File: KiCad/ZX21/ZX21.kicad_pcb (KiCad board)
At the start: 2 copper layers, 142 x 100 mm, 104 parts, among them IC1 ULA 2C210E, IC101 555, IC2 AT28C256, IC3 Z80A, IC301 3V3 PSU, IC303 AZ1117-3.3, IC4 62256, IC501 YM2149, IC502 GAL16V8, J1 Jack-DC, J203 Conn_01x03, J204 Conn_01x03, J301 Conn_01x04, J401 DB9_Male, J501 Conn_01x05, J502 Conn_01x08, J503 Conn_01x08, J504 Conn_01x07, J601 Conn_02x08_Odd_Even, J701 Conn_02x23_Row_Letter_First, J702 Conn_01x09, J703 Conn_01x09, X1 3.5MHz

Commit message: Diodes fixed
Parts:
- added D1: 1N4148, Diodes_THT:D_DO-35_SOD27_P7.62mm_Horizontal, F.Cu at (149.2, 118.1)
- added D101: 1N4148, Diodes_THT:D_DO-35_SOD27_P7.62mm_Horizontal, F.Cu at (43.2, 83.2)
- added D102: 1N4148, Diodes_THT:D_DO-35_SOD27_P7.62mm_Horizontal, F.Cu at (33.0, 83.2)
- added D2: 1N4148, Diodes_THT:D_DO-35_SOD27_P7.62mm_Horizontal, F.Cu at (151.8, 118.1)
- added D3: 1N4148, Diodes_THT:D_DO-35_SOD27_P7.62mm_Horizontal, F.Cu at (154.3, 118.1)
- added D4: 1N4148, Diodes_THT:D_DO-35_SOD27_P7.62mm_Horizontal, F.Cu at (156.8, 118.1)
- added D5: 1N4148, Diodes_THT:D_DO-35_SOD27_P7.62mm_Horizontal, F.Cu at (159.4, 118.1)
- added D6: 1N4148, Diodes_THT:D_DO-35_SOD27_P7.62mm_Horizontal, F.Cu at (161.9, 118.1)
- added D7: 1N4148, Diodes_THT:D_DO-35_SOD27_P7.62mm_Horizontal, F.Cu at (157.5, 118.7)
- added D8: 1N4148, Diodes_THT:D_DO-35_SOD27_P7.62mm_Horizontal, F.Cu at (167.0, 118.7)
- moved R28 245.5 mm to (161.9, 54.0)
- moved R33 165.0 mm to (73.0, 32.4)
- moved C7 164.3 mm to (83.2, 0.00)
- moved R4 147.0 mm to (97.2, 29.8)
- moved C10 142.1 mm to (103.6, 34.3)
- moved C6 136.9 mm to (78.1, 20.3)
- moved R101 130.7 mm to (62.2, 76.8), turned to 180 degrees
- moved R5 127.2 mm to (92.7, 19.1)
- moved C1 126.5 mm to (92.7, 95.2)
- moved C5 124.6 mm to (108.0, 90.8), turned to 270 degrees
- moved C2 105.2 mm to (9.53, 36.2)
- moved R103 89.7 mm to (56.5, 70.5)
- moved C103 73.6 mm to (47.6, 80.0)
- moved C12 70.3 mm to (53.3, 106.7), turned to 180 degrees
- moved C104 68.5 mm to (41.9, 78.7)
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
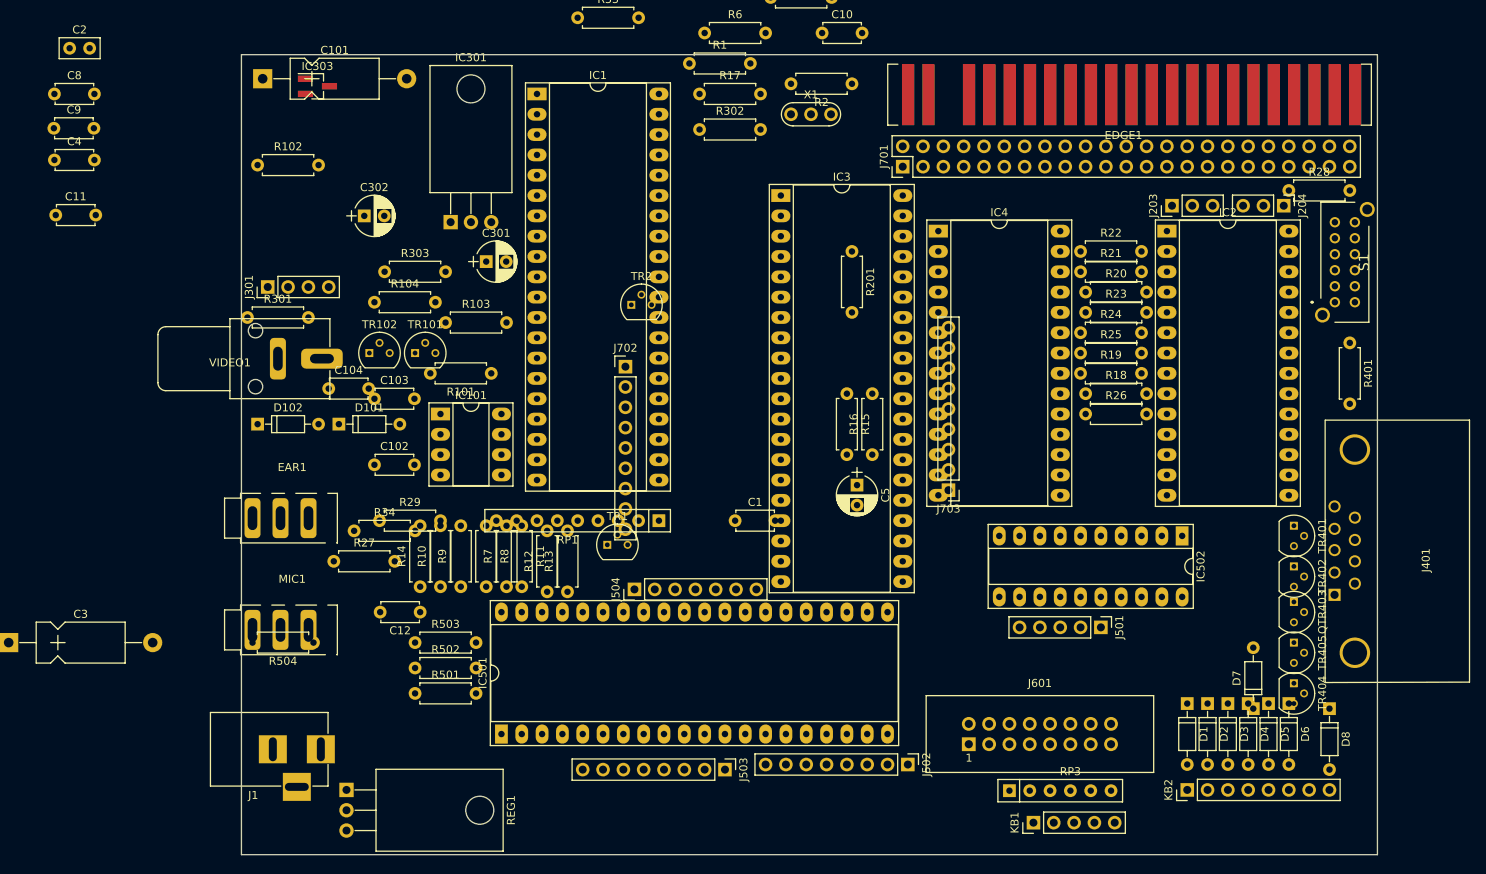
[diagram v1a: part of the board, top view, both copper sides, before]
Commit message: Added mounring holes
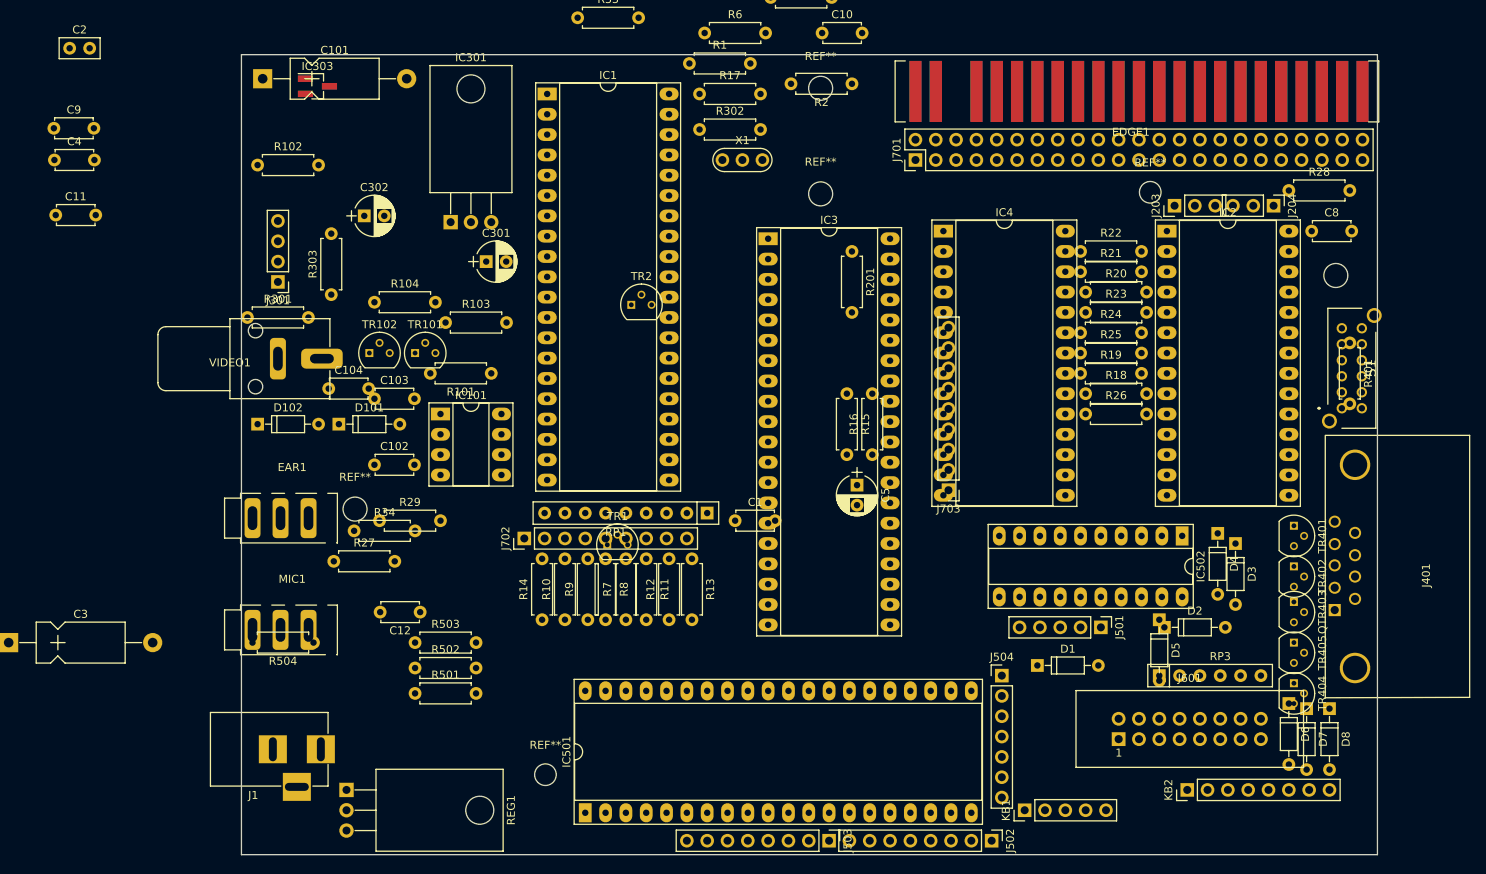
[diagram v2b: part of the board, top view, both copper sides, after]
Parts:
- added REF**: MountingHole_3mm, Mounting_Holes:MountingHole_3mm, F.Cu at (45.2, 93.8)
- added REF**: MountingHole_2.7mm, Mounting_Holes:MountingHole_2.7mm, F.Cu at (69.0, 127.0)
- added REF**: MountingHole_3mm, Mounting_Holes:MountingHole_3mm, F.Cu at (103.4, 54.4)
- added REF**: MountingHole_3mm, Mounting_Holes:MountingHole_3mm, F.Cu at (103.4, 41.2)
- added REF**: MountingHole_2.7mm, Mounting_Holes:MountingHole_2.7mm, F.Cu at (144.6, 54.2)
- added REF**: MountingHole_3mm, Mounting_Holes:MountingHole_3mm, F.Cu at (167.8, 64.6)
- moved C8 158.1 mm to (164.8, 59.1)
- moved J504 47.2 mm to (126.0, 114.6), turned to 0 degrees
- moved J702 24.9 mm to (66.4, 97.5), turned to 90 degrees
- moved RP3 23.6 mm to (145.7, 114.6)
- moved D4 21.6 mm to (153.0, 96.8)
- moved D3 20.0 mm to (155.3, 98.1)
- moved D1 19.3 mm to (130.5, 113.3), turned to 0 degrees
- moved J601 18.7 mm to (140.7, 122.6)
- moved D5 17.2 mm to (145.7, 107.6)
- moved R9 16.4 mm to (74.3, 107.6)
- moved R13 16.1 mm to (87.3, 100.0), turned to 270 degrees
- moved R10 16.1 mm to (71.4, 107.6)
- moved R11 16.1 mm to (81.6, 100.0)
- moved R14 15.8 mm to (68.6, 107.6)
- moved J503 15.8 mm to (104.5, 135.3)
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
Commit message: Placement getting there
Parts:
- removed REF** (x4): MountingHole_3mm, Mounting_Holes:MountingHole_3mm
- removed REF** (x2): MountingHole_2.7mm, Mounting_Holes:MountingHole_2.7mm
- added C303: 10N, Capacitors_SMD:C_0603_HandSoldering, F.Cu at (44.5, 46.0)
- added IC302: ESP32-WROOM, ESP32-footprints-Lib:ESP32-WROOM, B.Cu at (42.0, 49.8)
- added IC801: AS6C4008Extra, zxbus:DIP-4_W15.24mm_Socket_LongPads, F.Cu at (114.0, 57.5)
- added TR403: 2N3904, TO_SOT_Packages_THT:TO-92_Molded_Narrow, F.Cu at (169.9, 121.9)
- J701: footprint Pin_Headers:Pin_Header_Straight_2x23_Pitch2.54mm -> zxbus:Pin_Header_Straight_2x23_Pitch2.54mm
- moved C9 125.3 mm to (132.4, 57.2), turned to 270 degrees
- moved C4 101.8 mm to (109.2, 56.8), turned to 180 degrees
- moved C10 85.1 mm to (49.8, 100.3), turned to 180 degrees
- moved C2 77.4 mm to (86.7, 42.0), turned to 270 degrees
- moved R30 59.8 mm to (87.9, 87.6), turned to 90 degrees
- moved C7 59.5 mm to (100.0, 57.1), turned to 90 degrees
- moved R33 58.2 mm to (66.4, 90.2), turned to 180 degrees
- moved C11 52.9 mm to (38.7, 100.0), turned to 180 degrees
- moved C3 44.6 mm to (44.8, 122.9)
- moved C5 43.5 mm to (108.9, 47.3), turned to 180 degrees
- moved C101 42.4 mm to (63.5, 70.2), turned to 90 degrees
- moved R1 42.1 mm to (91.1, 80.0), turned to 270 degrees
- moved R201 41.8 mm to (148.3, 53.0), turned to 180 degrees
- moved R102 40.2 mm to (44.8, 89.2)
- moved D8 35.9 mm to (131.1, 117.5)
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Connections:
- net Net-(C302-Pad1) renamed +3V3
- IC303 pad 3: +9V -> +5V

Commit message: Add Gate
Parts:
- removed the TR403 at (169.9, 121.9)
- added C105: 100N, Capacitors_SMD:C_0603_HandSoldering, F.Cu at (123.2, 68.6)
- added IC102: 74HCT00, Housings_SOIC:SOIC-14_3.9x8.7mm_Pitch1.27mm, B.Cu at (121.6, 74.0)
- added J2: Conn_01x02, Pin_Headers:Pin_Header_Straight_1x02_Pitch2.54mm, B.Cu at (133.0, 93.7)
- added R105: 4K7, Resistors_SMD:R_0603_HandSoldering, B.Cu at (123.5, 67.0)
- renumbered QTR403 to TR403
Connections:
- IC4 pad 2: A12 -> Net-(IC102-Pad6)
- IC4 pad 21: A10 -> Net-(IC102-Pad11)
- IC4 pad 23: A11 -> Net-(IC102-Pad8)
- IC4 pad 26: A13 -> Net-(IC102-Pad3)
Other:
- net class Default: clearance 0.2 -> 0.2032; trace_width 0.25 -> 0.2032; via_dia 0.8 -> 0.6858
- rule trace_clearance: 0.2 -> 0.2032

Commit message: Part way through routing
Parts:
- added REF**: MountingHole_3mm, Mounting_Holes:MountingHole_3mm, F.Cu at (69.0, 127.0)
- added REF**: MountingHole_3mm, Mounting_Holes:MountingHole_3mm, F.Cu at (45.2, 93.8)
- added REF**: MountingHole_3mm, Mounting_Holes:MountingHole_3mm, F.Cu at (103.4, 54.4)
- added REF**: MountingHole_3mm, Mounting_Holes:MountingHole_3mm, F.Cu at (103.4, 41.2)
- added REF**: MountingHole_2.7mm, Mounting_Holes:MountingHole_2.7mm, F.Cu at (144.6, 54.0)
- added REF**: MountingHole_3mm, Mounting_Holes:MountingHole_3mm, F.Cu at (167.8, 64.6)
- added X501: ECS-100AX-040, Oscillators:Oscillator_DIP-14, F.Cu at (64.8, 117.3)
- J501: value Conn_01x05 -> Conn_01x06; footprint Pin_Headers:Pin_Header_Straight_1x05_Pitch2.54mm -> Pin_Headers:Pin_Header_Straight_1x06_Pitch2.54mm
- moved R28 98.9 mm to (66.4, 72.4), turned to 270 degrees
- moved R302 42.0 mm to (50.8, 65.4), turned to 270 degrees
- moved R201 38.5 mm to (185.7, 61.9)
- moved R301 22.2 mm to (44.5, 78.1), turned to 90 degrees
- moved C105 18.2 mm to (125.4, 86.7)
- moved R105 18.2 mm to (125.6, 85.1)
- moved R16 16.6 mm to (113.3, 103.2), turned to 270 degrees
- moved TR404 9.95 mm to (171.1, 120.7), turned to 180 degrees
- moved J204 8.90 mm to (170.8, 56.5)
- moved TR401 5.96 mm to (157.4, 98.9)
- moved IC102 5.54 mm to (123.8, 79.1)
- moved TR102 4.32 mm to (52.1, 94.9), turned to 90 degrees
- moved C102 3.72 mm to (61.3, 88.9)
- moved TR101 3.38 mm to (49.2, 74.9), turned to 270 degrees
- moved R2 3.31 mm to (122.6, 54.3)
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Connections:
- IC2 pad 28: VCC -> +5V
- IC4 pad 28: VCC -> +5V
- IC502 pad 20: VCC -> +5V
- J501 pad 1: Net-(IC502-Pad16) -> Net-(IC502-Pad17)
- J501 pad 2: Net-(IC502-Pad15) -> Net-(IC502-Pad16)
- J501 pad 3: Net-(IC502-Pad14) -> Net-(IC502-Pad15)
- J501 pad 4: Net-(IC502-Pad13) -> Net-(IC502-Pad14)
- J501 pad 5: Net-(IC502-Pad12) -> Net-(IC502-Pad13)
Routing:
- net GND: track 0.00 -> 459.1 mm
- net +5V: track 0.00 -> 301.9 mm
- net +9V: track 0.00 -> 191.7 mm
- net KBD0: track 0.00 -> 184.9 mm
- net KBD2: track 0.00 -> 160.3 mm
- net KBD1: track 0.00 -> 152.1 mm
- net KBD4: track 0.00 -> 149.5 mm
- net KBD3: track 0.00 -> 147.3 mm
- net A12: track 0.00 -> 139.0 mm, vias 0 -> 1
- net D4': track 0.00 -> 125.7 mm, vias 0 -> 1
- net A2: track 0.00 -> 124.7 mm, vias 0 -> 2
- net D2': track 0.00 -> 123.0 mm
- net D0': track 0.00 -> 121.6 mm
- net D1': track 0.00 -> 121.5 mm
- net D3': track 0.00 -> 121.5 mm, vias 0 -> 1
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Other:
- board text added: "BOTTOM"
- board text added: "TOP"

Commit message: Yet more routing!
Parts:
- moved C8 40.4 mm to (152.4, 98.7)
- moved C303 13.3 mm to (57.2, 42.2), turned to 180 degrees
- moved IC303 10.5 mm to (57.7, 44.8), turned to 0 degrees
- moved R201 6.93 mm to (183.8, 55.2)
- moved C302 6.48 mm to (59.4, 45.7), turned to 270 degrees
- moved C9 1.92 mm to (134.3, 57.5)
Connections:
- IC102 pad 10: A11 -> Net-(IC102-Pad1)
- IC102 pad 12: Net-(IC102-Pad1) -> A10
- IC102 pad 13: A10 -> Net-(IC102-Pad1)
- IC102 pad 9: Net-(IC102-Pad1) -> A11
- IC501 pad 28: (no net) -> Net-(IC501-Pad28)
- IC502 pad 1: CLK -> MREQ
- IC502 pad 11: IORQ -> A15
- IC502 pad 17: Net-(IC501-Pad22) -> Net-(IC502-Pad17)
- IC502 pad 7: A5 -> A7
- IC502 pad 8: A7 -> WR
- IC502 pad 9: WR -> IORQ
- J504 pad 2: Net-(IC501-Pad25) -> Net-(J504-Pad2)
- J504 pad 3: Net-(IC501-Pad24) -> Net-(IC501-Pad28)
- J504 pad 4: Net-(IC501-Pad29) -> Net-(IC501-Pad25)
- J504 pad 5: Net-(IC501-Pad26) -> Net-(IC501-Pad24)
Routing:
- net A13: track 12.4 -> 197.3 mm, vias 0 -> 4
- net A11: track 55.0 -> 171.3 mm, vias 1 -> 5
- net A14: track 73.4 -> 175.0 mm, vias 1 -> 5
- net A10: track 35.1 -> 108.3 mm, vias 1 -> 3
- net A15: track 47.9 -> 117.5 mm, vias 0 -> 2
- net A9: track 74.8 -> 144.1 mm, vias 0 -> 2
- net A8: track 70.1 -> 133.7 mm, vias 1 -> 5
- net A12: track 139.0 -> 193.9 mm, vias 1 -> 3
- net A4: track 91.3 -> 143.8 mm, vias 1 -> 2
- net A5: track 93.7 -> 140.1 mm
- net A3: track 91.5 -> 137.1 mm, vias 1 -> 2
- net Net-(IC501-Pad29): track 0.95 -> 41.4 mm
- net Net-(IC501-Pad27): track 0.00 -> 37.3 mm
- net A1: track 96.8 -> 133.0 mm
- net GND: track 459.1 -> 491.8 mm, vias 0 -> 1
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
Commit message: Even more routing
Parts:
- C105, C303, IC303, J504: moved to B.Cu
- J2: moved to F.Cu
- moved R16 47.1 mm to (110.8, 56.2), turned to 90 degrees
- moved C9 39.6 mm to (117.5, 21.6)
- moved R201 27.3 mm to (156.5, 54.9)
- moved R2 21.0 mm to (120.7, 33.3)
- moved R15 15.1 mm to (108.3, 40.6), turned to 270 degrees
- moved IC303 6.42 mm to (63.6, 47.3)
- moved C5 4.44 mm to (104.4, 47.3)
- moved C302 1.27 mm to (58.1, 45.7)
- moved R105 0.47 mm to (125.1, 85.1)
- moved R28 0.45 mm to (66.7, 72.7)
- turned J2 to 90 degrees
- turned J504 to 270 degrees
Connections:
- IC102 pad 14: (no net) -> +5V
- IC102 pad 7: (no net) -> GND
- IC3 pad 25: BUSAK -> BUSRQ
- R16 pad 1: BUSAK -> BUSRQ
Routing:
- net RD: track 9.53 -> 153.1 mm, vias 0 -> 2
- net ROM_CS: track 43.3 -> 175.1 mm, vias 0 -> 4
- net BUSAK: track 9.62 -> 129.4 mm, vias 0 -> 3
- net BUSRQ: track 9.53 -> 128.1 mm, vias 0 -> 3
- net INT: track 9.62 -> 127.3 mm, vias 0 -> 3
- net MREQ: track 76.2 -> 193.4 mm, vias 0 -> 2
- net RFSH: track 9.53 -> 124.3 mm, vias 0 -> 4
- net MI: track 9.60 -> 122.1 mm, vias 0 -> 4
- net NMI: track 13.9 -> 104.6 mm, vias 0 -> 4
- net HALT: track 17.3 -> 101.2 mm, vias 0 -> 1
- net RAM_CS: track 9.62 -> 81.0 mm, vias 0 -> 4
- net RESET: track 9.62 -> 76.5 mm, vias 0 -> 2
- net +5V: track 295.7 -> 356.8 mm
- net A7: track 76.0 -> 131.4 mm
- net A5: track 140.1 -> 90.9 mm
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- added copper zone on F.Cu, net GND

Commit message: 3 SD working better
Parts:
- IC1, IC3, IC501: footprint Housings_DIP:DIP-40_W15.24mm_Socket_LongPads -> zxbus:DIP-40_W15.24mm_Socket_LongPads
- IC2, IC4: footprint Housings_DIP:DIP-28_W15.24mm_Socket_LongPads -> zxbus:DIP-28_W15.24mm_Socket_LongPads
